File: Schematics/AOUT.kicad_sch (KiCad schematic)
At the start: 0 parts

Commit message: Added recommended op-amps
Added recommended op-amps (without values) with dual mono TS in and out
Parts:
- added C29, C32, C37: C_Polarized, symbol Device:C_Polarized
- added C30, C31, C33, C34, C35, C36: C, symbol Device:C
- added J4, J5: AudioJack2_Switch, symbol Connector_Audio:AudioJack2_Switch
- added Q1, Q2: Q_NPN_BEC, symbol Device:Q_NPN_BEC
- added R31, R32, R33, R34, R35, R36: R, symbol Device:R
- added U3: Opamp_Dual, symbol Device:Opamp_Dual
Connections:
- new net: C36.2, C37.1, R36.2, U3.7
- new net: C37.2, Q2.3 (C)
- new net: C33.1, R31.2, U3.2 (-)
- new net: C32.1, C33.2, R33.2, U3.1
- new net: C34.1, R34.2, R35.1, R36.1
- new net: C36.1, R35.2, U3.6 (-)
- new net: J4.S, J4.SN, Q1.2 (E)
- new net: C32.2, Q1.3 (C)
- new net: C31.1, R31.1, R32.2, R33.1
- new net: C29.1, U3.8 (V+)
- new net: J5.S, J5.SN, Q2.2 (E)
- new net GND: C29.2, C30.2, C31.2, C34.2, C35.2, J4.T, J4.TN, J5.T, J5.TN, U3.4 (V-)
- new net VCOM: C30.1, C35.1, U3.3 (+), U3.5 (+)
- new net V_{OUT}L: R32.1
- new net V_{OUT}R: R34.1
- new net ZEROL: Q1.1 (B)
- new net ZEROR: Q2.1 (B)

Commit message: Input Buffer & EEPROM
line and instrument level buffers for the input added. EEPROM added and credits attributed !
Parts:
- C29: value C_Polarized -> 100n
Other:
- note added: "Drawn by Harvey McBurney"
- title: (none) -> Audio Output Buffers
- moved on the sheet: C30, C31, C32, C33, C34, C35, C36, C37, J4, J5, Q1, Q2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

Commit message: Schematic Update
Added EEPROM connections
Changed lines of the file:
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@@
 		)
 	)
-	(text_box "Separate L/R TS\nMono Outputs"
+	(text_box "TS Mono \nLine Out"
 		(exclude_from_sim no)
 		(at 182.245 53.975 0)
-		(size 20.32 88.9)
+		(size 20.32 29.845)
 		(stroke
 			(width 0)
@@
 		(stroke
 			(width 0)
+			(type default)
+		)
+		(fill
+			(type none)
+		)
+		(effects
+			(font
+				(size 1.27 1.27)
+			)
+			(justify left top)
+		)
+	)
+	(text_box "TS Mono \nInst Out"
+		(exclude_from_sim no)
+		(at 182.88 114.3 0)
+		(size 20.32 29.845)
+		(stroke
+			(width 0)

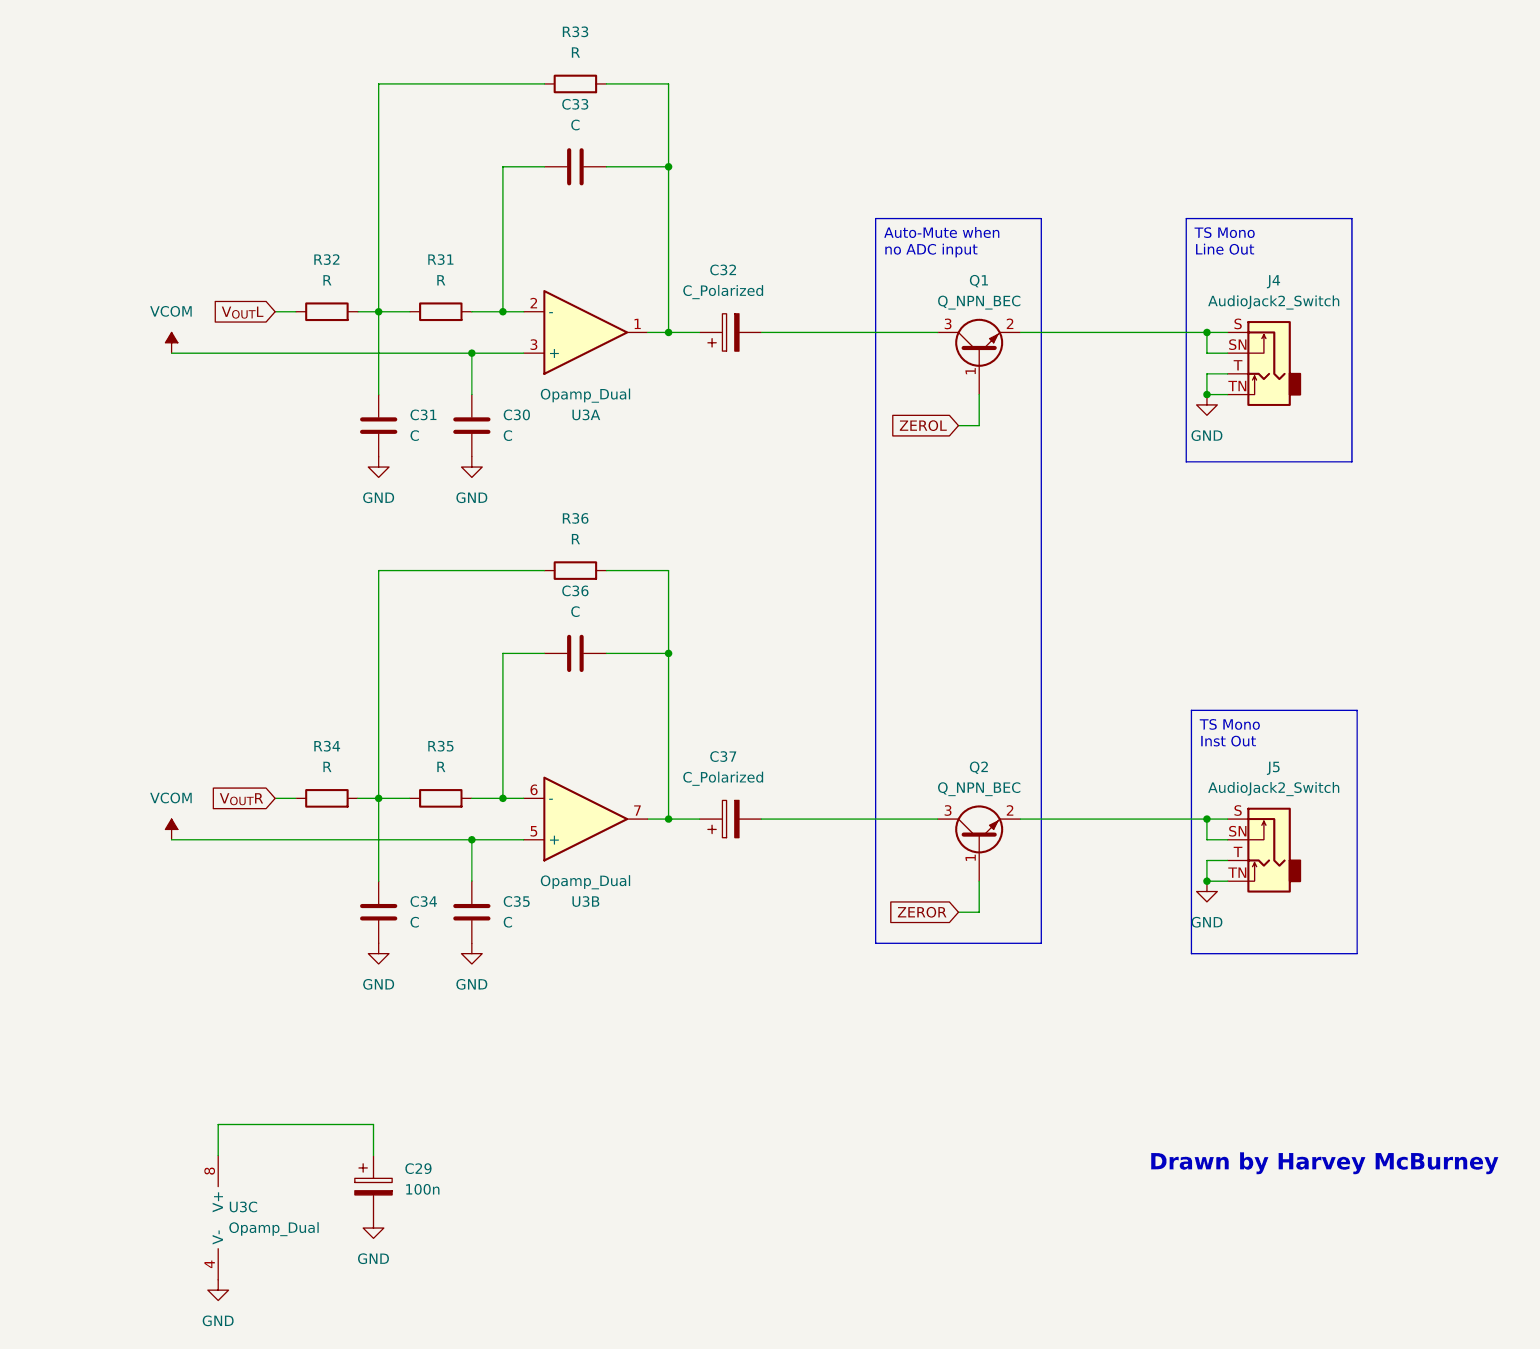
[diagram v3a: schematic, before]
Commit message: Started adding footprints, changed values.
Added footprints for most components. need to check in uni which sizes are available and what will need to be ordered from mouser.
Changed line in/out to TRS as this will be more reliable and added 0 ohm resistor options to bypass mono input and use line in/out as stereo.
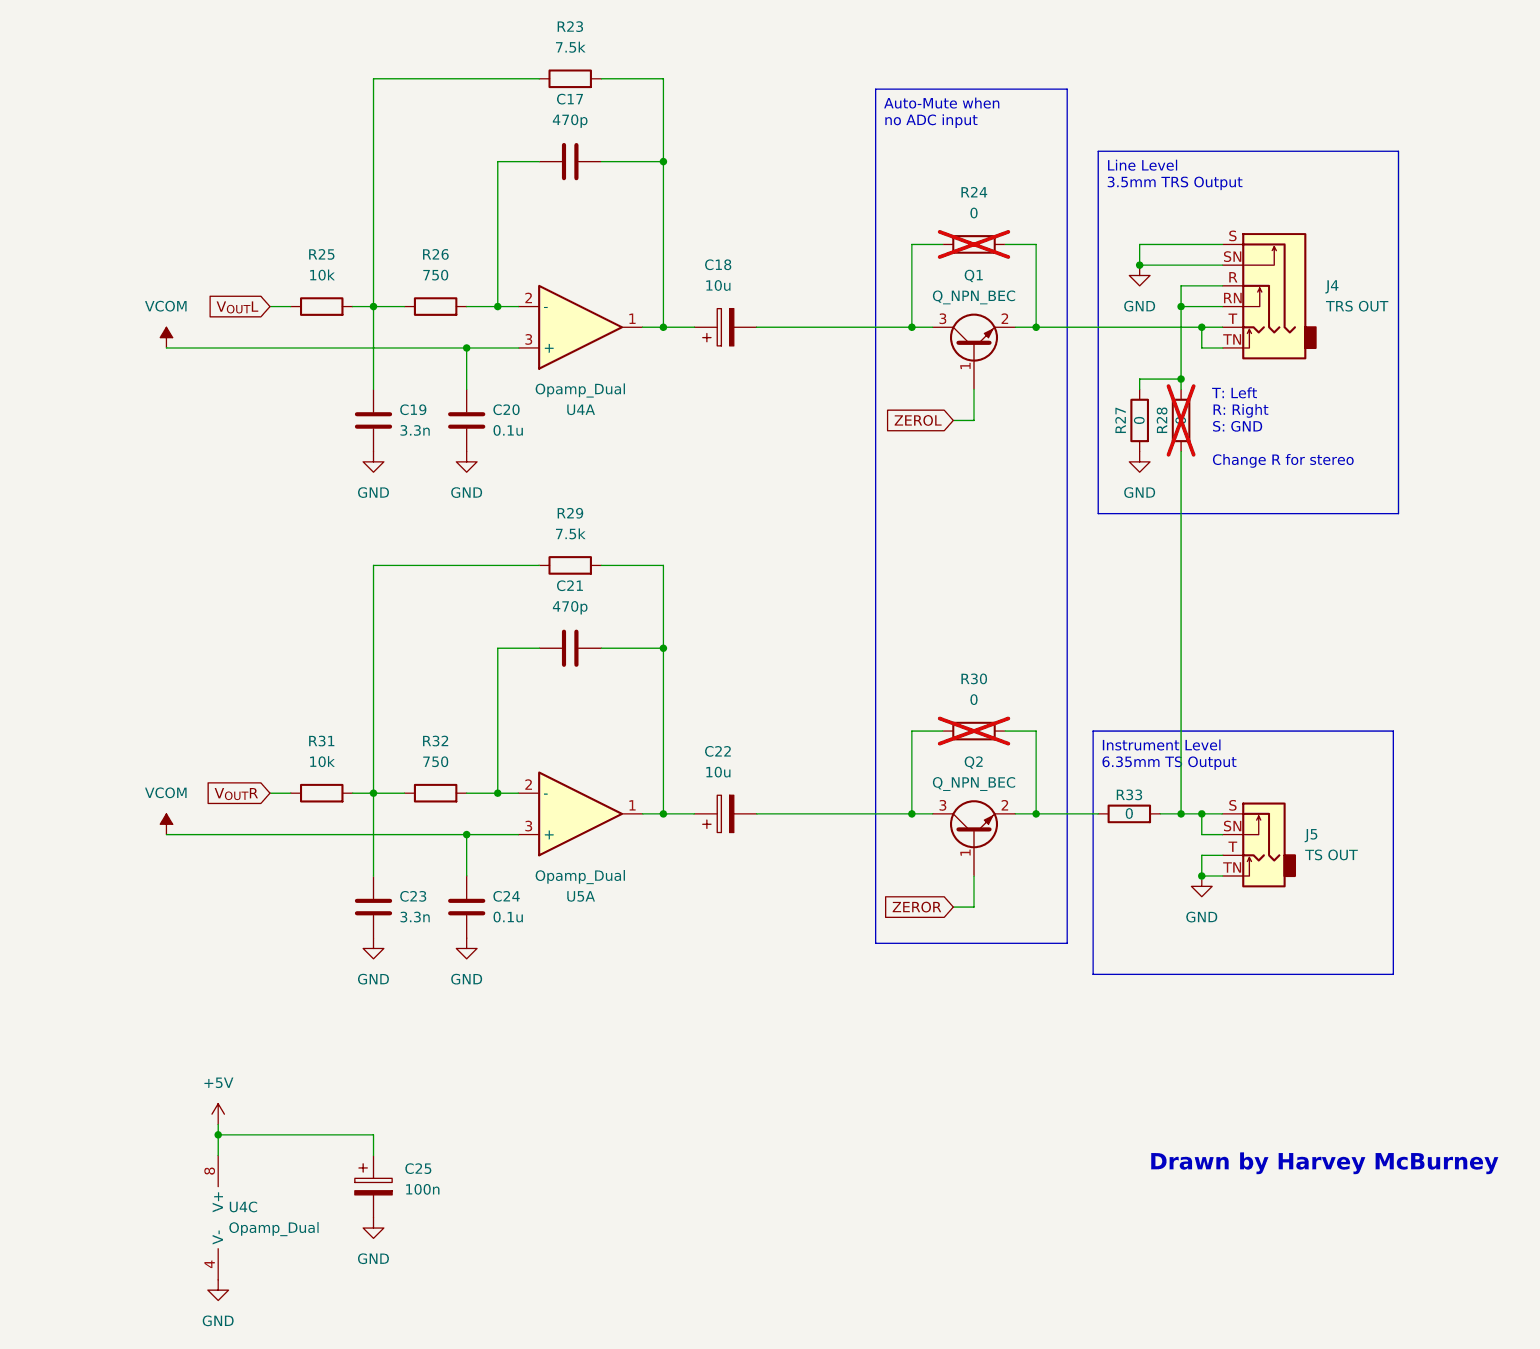
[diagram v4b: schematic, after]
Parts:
- removed C34, C35, C36: C, symbol Device:C
- removed C37: C_Polarized, symbol Device:C_Polarized
- removed J4: AudioJack2_Switch, symbol Connector_Audio:AudioJack2_Switch
- removed R34, R35, R36: R, symbol Device:R
- removed unit 2 of U3
- added C21: 470p, symbol Device:C
- added C22: 10u, symbol Device:C_Polarized
- added C23: 3.3n, symbol Device:C
- added C24: 0.1u, symbol Device:C
- added J4: TRS OUT, symbol Connector_Audio:AudioJack3_Switch
- added R24, R27, R28, R30, R33: 0, Resistor_SMD:R_0603_1608Metric_Pad0.98x0.95mm_HandSolder, symbol Device:R
- added R29: 7.5k, Resistor_SMD:R_0603_1608Metric_Pad0.98x0.95mm_HandSolder, symbol Device:R
- added R31: 10k, Resistor_SMD:R_0603_1608Metric_Pad0.98x0.95mm_HandSolder, symbol Device:R
- added R32: 750, Resistor_SMD:R_0603_1608Metric_Pad0.98x0.95mm_HandSolder, symbol Device:R
- added U5: Opamp_Dual, symbol Device:Opamp_Dual
- C17: renamed from C33; value C -> 470p
- C18: renamed from C32; value C_Polarized -> 10u
- C19: renamed from C31; value C -> 3.3n
- C20: renamed from C30; value C -> 0.1u
- J5: value AudioJack2_Switch -> TS OUT; footprint (none) -> Connector_Audio:Jack_6.35mm_Neutrik_NMJ4HHD2_Horizontal
- Q1, Q2: footprint (none) -> Package_TO_SOT_THT:TO-220-3_Vertical
- R23: renamed from R33; value R -> 7.5k; footprint (none) -> Resistor_SMD:R_0603_1608Metric_Pad0.98x0.95mm_HandSolder
- R25: renamed from R32; value R -> 10k; footprint (none) -> Resistor_SMD:R_0603_1608Metric_Pad0.98x0.95mm_HandSolder
- R26: renamed from R31; value R -> 750; footprint (none) -> Resistor_SMD:R_0603_1608Metric_Pad0.98x0.95mm_HandSolder
- renumbered C29 to C25, U3 to U4
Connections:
- net GND: now also C23.2, C24.2, J4.S, J4.SN, R27.2
- net VCOM: now also C24.1, U5.3 (+)
- net V_{OUT}R: now also R31.1
- net at Q2.3 (C): now also C22.2, R30.1
- net at Q1.2 (E): now also J4.T, J4.TN, R24.2
- net at C18.2, Q1.3 (C): now also R24.1
- net +5V: now reaches C25.1, U4.8 (V+)
- net at J5.S, J5.SN: now also R28.2, R33.2; no longer Q2.2 (E)
- new net: C21.2, C22.1, R29.2, U5.1
- new net: J4.R, J4.RN, R27.1, R28.1
- new net: C23.1, R29.1, R31.2, R32.1
- new net: C21.1, R32.2, U5.2 (-)
- new net: Q2.2 (E), R30.2, R33.1
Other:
- note added: "T: Left R: Right S: GND Change R for stereo"
- moved on the sheet: C17, C18, C19, C20, R23, R25, R26, U4A

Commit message: Updated to KiCAD v9
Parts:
- removed J4: TRS OUT, symbol Connector_Audio:AudioJack3_Switch
- added J10: Line Out, Connector_Audio:Jack_3.5mm_CUI_SJ1-3523N_Horizontal, symbol Connector_Audio:AudioJack3
- C18, C22: footprint (none) -> Capacitor_SMD:CP_Elec_5x5.4
- C25: value 100n -> 0.1u
- J5: value TS OUT -> Inst Out
- renumbered U5 to U4
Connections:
- net GND: now also J10.S
- net VCOM: now also U4.5 (+); no longer U4.3 (+)
- net at C21.2, C22.1, R29.2: now also U4.7; no longer U4.1
- net at R27.1, R28.1: now also J10.R
- net at C21.1, R32.2: now also U4.6 (-); no longer U4.2 (-)
- net at Q1.2 (E), R24.2: now also J10.T
